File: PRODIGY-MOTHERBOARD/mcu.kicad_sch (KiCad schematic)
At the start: 19 parts, among them J1 USB_C_Receptacle, J2 Bus_M.2_Socket_B, SW1 SW_Push_Dual_x2

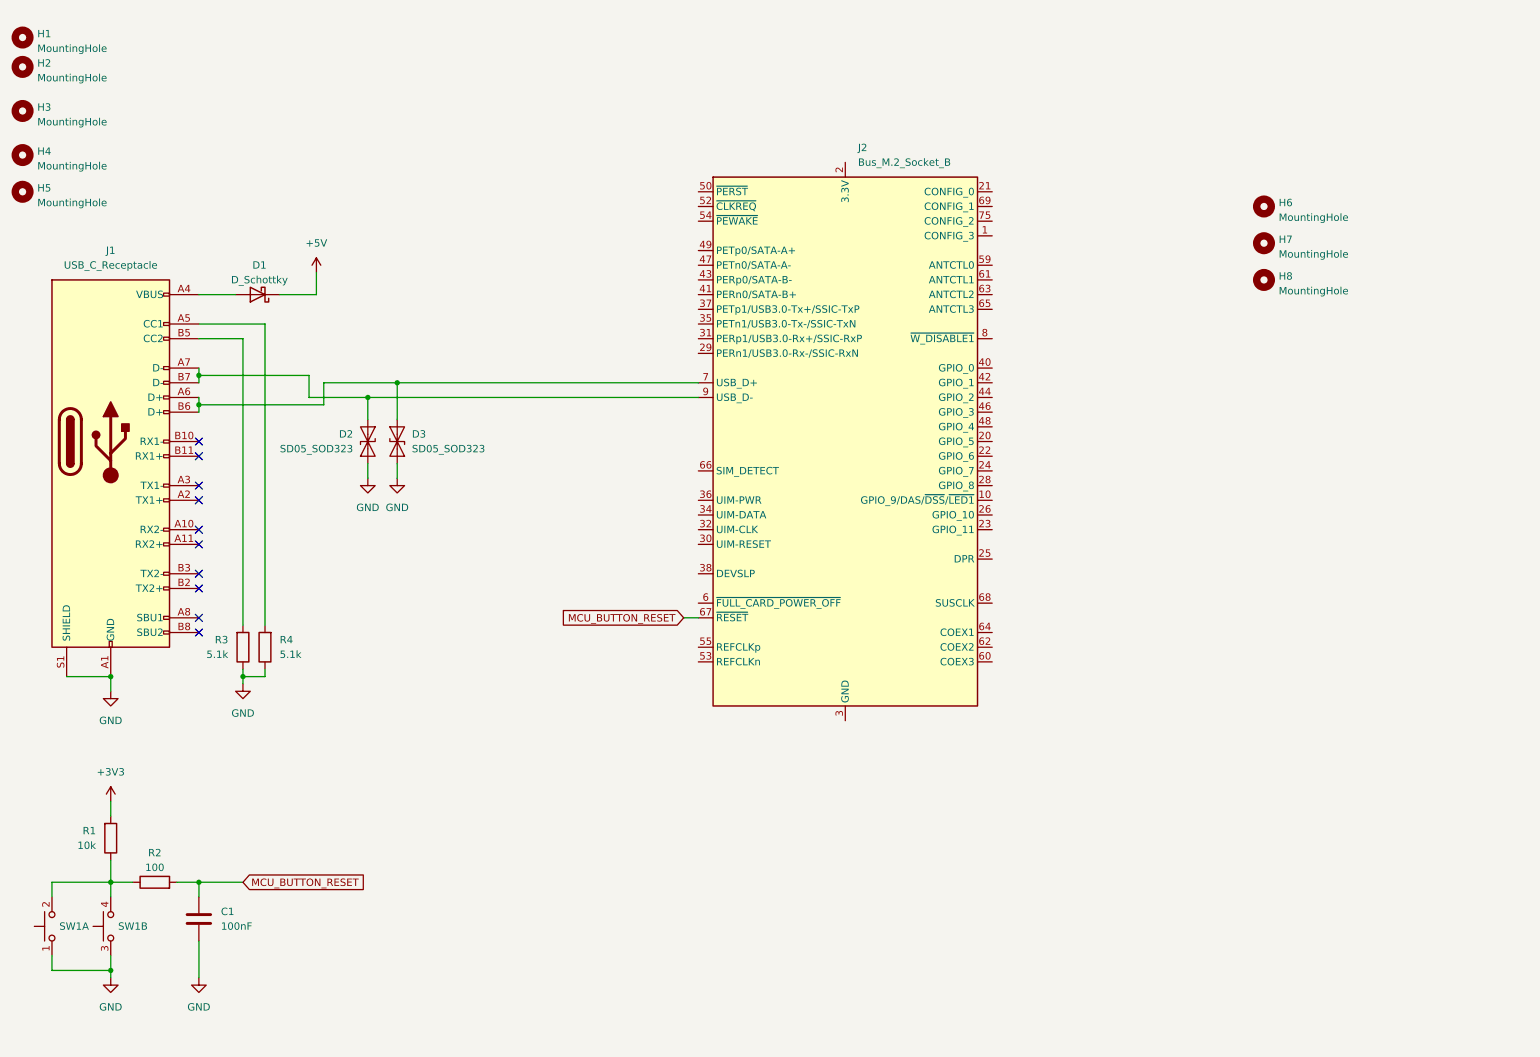
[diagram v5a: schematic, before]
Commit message: Added pins to MCU. Added Decoder for SPI SS-Multiplexing.
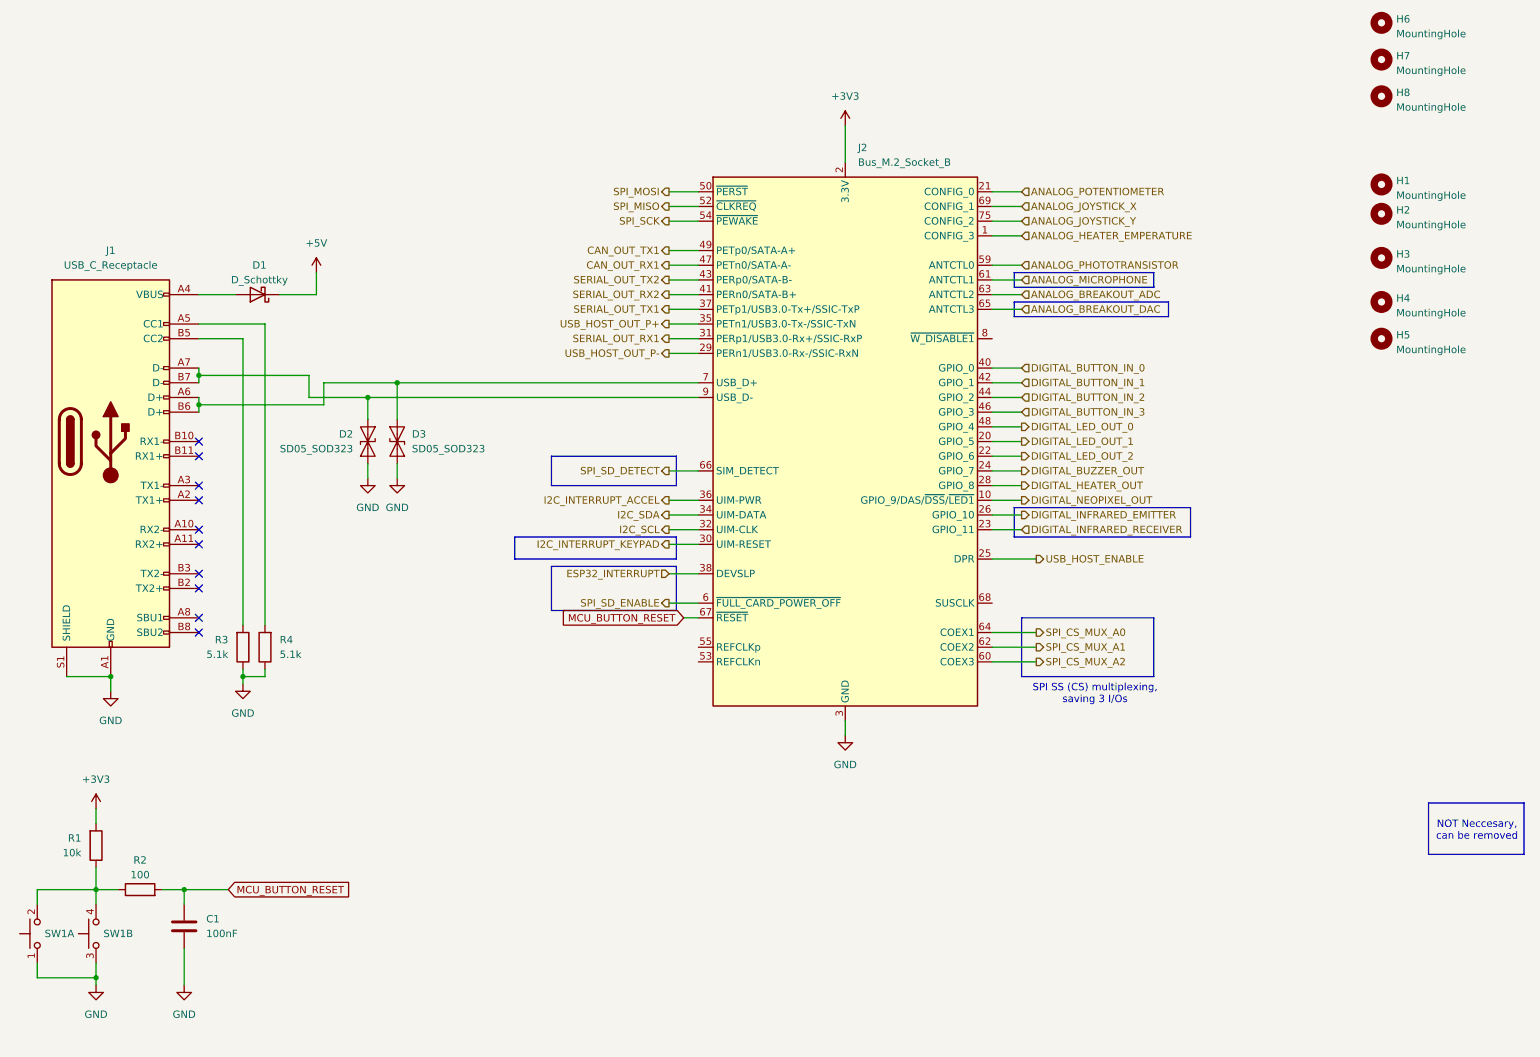
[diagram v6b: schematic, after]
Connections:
- net +3V3: now also J2.2 (3.3V), J2.4 (3.3V), J2.70 (3.3V), J2.72 (3.3V), J2.74 (3.3V)
- net GND: now also J2.11 (GND), J2.27 (GND), J2.3 (GND), J2.33 (GND), J2.39 (GND), J2.45 (GND), J2.5 (GND), J2.51 (GND), J2.57 (GND), J2.71 (GND), J2.73 (GND)
- net ANALOG_HEATER_EMPERATURE: now reaches J2.1 (CONFIG_3)
- net DIGITAL_NEOPIXEL_OUT: now reaches J2.10 (GPIO_9/DAS/~{DSS}/~{LED1})
- net DIGITAL_LED_OUT_1: now reaches J2.20 (GPIO_5)
- net ANALOG_POTENTIOMETER: now reaches J2.21 (CONFIG_0)
- net DIGITAL_LED_OUT_2: now reaches J2.22 (GPIO_6)
- net DIGITAL_INFRARED_RECEIVER: now reaches J2.23 (GPIO_11)
- net DIGITAL_BUZZER_OUT: now reaches J2.24 (GPIO_7)
- net USB_HOST_ENABLE: now reaches J2.25 (DPR)
- net DIGITAL_INFRARED_EMITTER: now reaches J2.26 (GPIO_10)
- net DIGITAL_HEATER_OUT: now reaches J2.28 (GPIO_8)
- net USB_HOST_OUT_P-: now reaches J2.29 (PERn1/USB3.0-Rx-/SSIC-RxN)
- net I2C_INTERRUPT_KEYPAD: now reaches J2.30 (UIM-RESET)
- net SERIAL_OUT_RX1: now reaches J2.31 (PERp1/USB3.0-Rx+/SSIC-RxP)
- net I2C_SCL: now reaches J2.32 (UIM-CLK)
- net I2C_SDA: now reaches J2.34 (UIM-DATA)
- net USB_HOST_OUT_P+: now reaches J2.35 (PETn1/USB3.0-Tx-/SSIC-TxN)
- net I2C_INTERRUPT_ACCEL: now reaches J2.36 (UIM-PWR)
- net SERIAL_OUT_TX1: now reaches J2.37 (PETp1/USB3.0-Tx+/SSIC-TxP)
- net ESP32_INTERRUPT: now reaches J2.38 (DEVSLP)
- net DIGITAL_BUTTON_IN_0: now reaches J2.40 (GPIO_0)
- net SERIAL_OUT_RX2: now reaches J2.41 (PERn0/SATA-B+)
- net DIGITAL_BUTTON_IN_1: now reaches J2.42 (GPIO_1)
- net SERIAL_OUT_TX2: now reaches J2.43 (PERp0/SATA-B-)
- net DIGITAL_BUTTON_IN_2: now reaches J2.44 (GPIO_2)
- net DIGITAL_BUTTON_IN_3: now reaches J2.46 (GPIO_3)
- net CAN_OUT_RX1: now reaches J2.47 (PETn0/SATA-A-)
- net DIGITAL_LED_OUT_0: now reaches J2.48 (GPIO_4)
- net CAN_OUT_TX1: now reaches J2.49 (PETp0/SATA-A+)
- net SPI_MOSI: now reaches J2.50 (~{PERST})
- net SPI_MISO: now reaches J2.52 (~{CLKREQ})
- net SPI_SCK: now reaches J2.54 (~{PEWAKE})
- net ANALOG_PHOTOTRANSISTOR: now reaches J2.59 (ANTCTL0)
- net SPI_SD_ENABLE: now reaches J2.6 (~{FULL_CARD_POWER_OFF})
- net SPI_CS_MUX_A2: now reaches J2.60 (COEX3)
- net ANALOG_MICROPHONE: now reaches J2.61 (ANTCTL1)
- net SPI_CS_MUX_A1: now reaches J2.62 (COEX2)
- net ANALOG_BREAKOUT_ADC: now reaches J2.63 (ANTCTL2)
- net SPI_CS_MUX_A0: now reaches J2.64 (COEX1)
- net ANALOG_BREAKOUT_DAC: now reaches J2.65 (ANTCTL3)
- net SPI_SD_DETECT: now reaches J2.66 (SIM_DETECT)
- net ANALOG_JOYSTICK_X: now reaches J2.69 (CONFIG_1)
- net ANALOG_JOYSTICK_Y: now reaches J2.75 (CONFIG_2)
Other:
- note added: "NOT Neccesary, can be removed"
- note added: "SPI SS (CS) multiplexing, saving 3 I/Os"
- moved on the sheet: C1, H1, H2, H3, H4, H5, H6, H7, H8, R1, R2, SW1A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

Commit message: Added proper debounce filter elements to buttons.
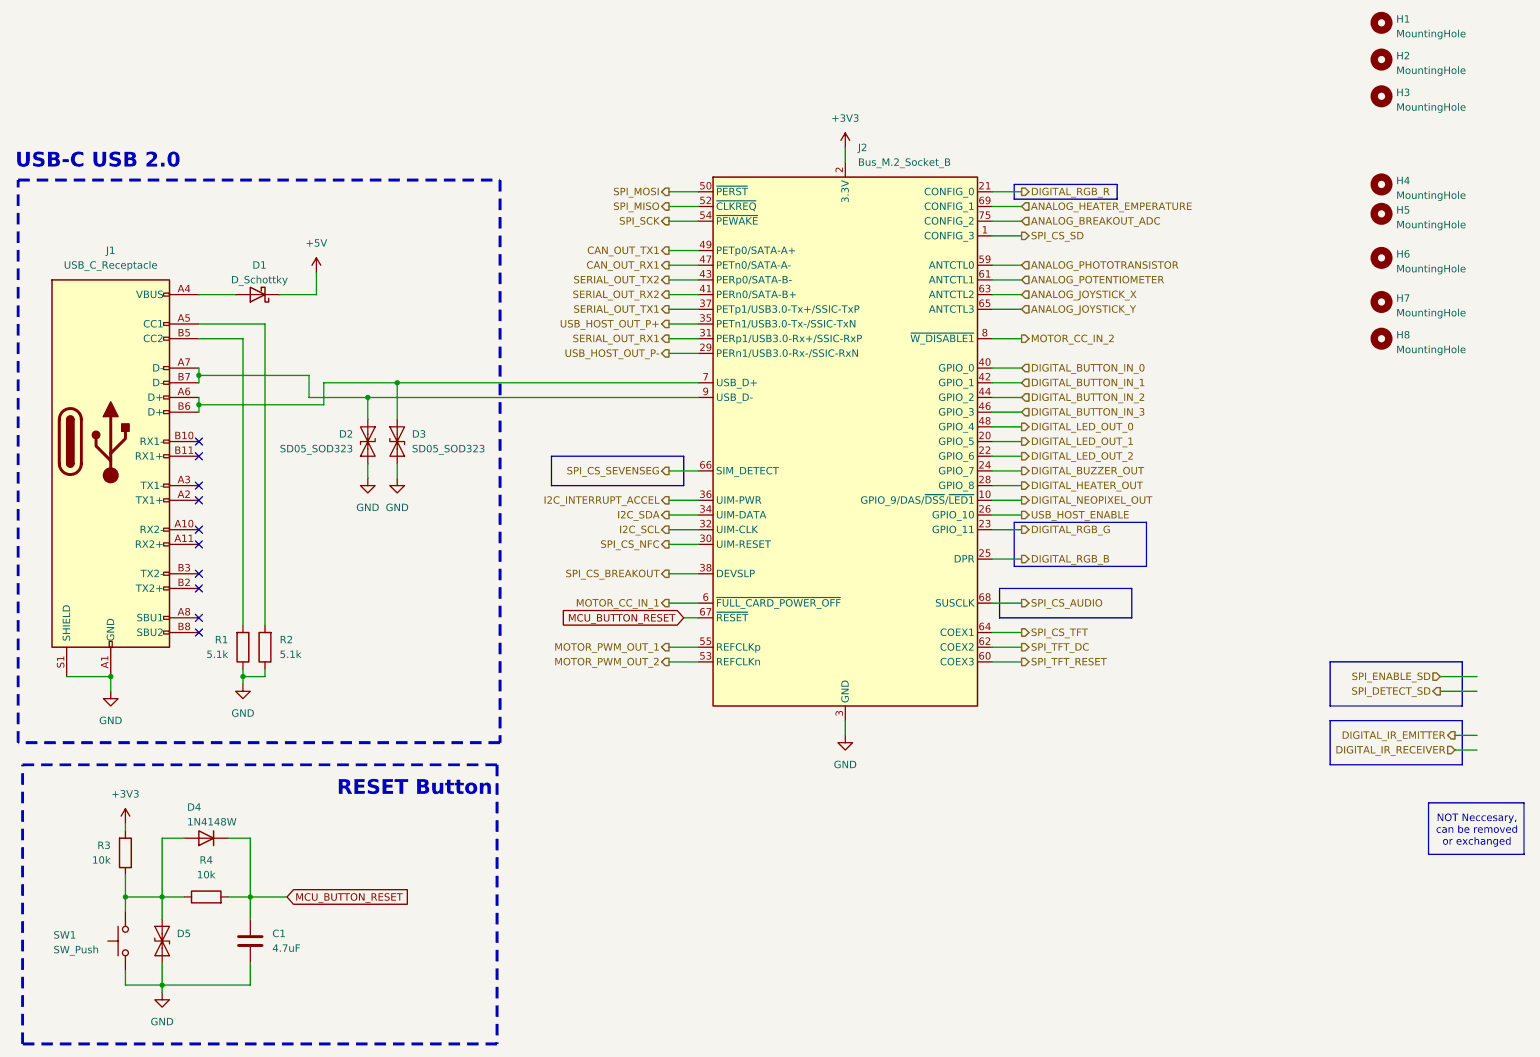
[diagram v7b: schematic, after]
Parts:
- removed R1: 10k, Resistor_SMD:R_0603_1608Metric, symbol Device:R
- removed R2: 100, Resistor_SMD:R_0603_1608Metric, symbol Device:R
- removed SW1: SW_Push_Dual_x2, symbol Switch:SW_Push_Dual_x2
- added D4: 1N4148W, Diode_SMD:D_SOD-123, symbol Diode:1N4148W
- added D5: SD05_SOD323, Diode_SMD:D_SOD-323, symbol Diode:SD05_SOD323
- added R3, R4: 10k, Resistor_SMD:R_0603_1608Metric, symbol Device:R
- added SW1: SW_Push, Button_Switch_SMD:SW_Push_1P1T_NO_CK_KMR2, symbol Switch:SW_Push
- C1: value 100nF -> 4.7uF
- renumbered H6 to H1, H7 to H2, H8 to H3, H1 to H4, H2 to H5, H3 to H6, H4 to H7, H5 to H8, R3 to R1, R4 to R2
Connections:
- net ANALOG_BREAKOUT_DAC is gone; now on net ANALOG_JOYSTICK_Y: J2.65 (ANTCTL3)
- net ANALOG_MICROPHONE is gone; now on net ANALOG_POTENTIOMETER: J2.61 (ANTCTL1)
- net DIGITAL_INFRARED_EMITTER is gone; now on net USB_HOST_ENABLE: J2.26 (GPIO_10)
- net +3V3: now also R3.2
- net ANALOG_BREAKOUT_ADC: now also J2.75 (CONFIG_2); no longer J2.63 (ANTCTL2)
- net ANALOG_HEATER_EMPERATURE: now also J2.69 (CONFIG_1); no longer J2.1 (CONFIG_3)
- net ANALOG_JOYSTICK_X: now also J2.63 (ANTCTL2); no longer J2.69 (CONFIG_1)
- net ANALOG_JOYSTICK_Y: no longer J2.75 (CONFIG_2)
- net ANALOG_POTENTIOMETER: no longer J2.21 (CONFIG_0)
- net GND: now also D5.1 (A1), SW1.1
- net MCU_BUTTON_RESET: now also D4.1 (K), R4.2
- net USB_HOST_ENABLE: no longer J2.25 (DPR)
- net MOTOR_PWM_OUT_2: now reaches J2.53 (REFCLKn)
- net MOTOR_PWM_OUT_1: now reaches J2.55 (REFCLKp)
- net SPI_CS_AUDIO: now reaches J2.68 (SUSCLK)
- net MOTOR_CC_IN_2: now reaches J2.8 (~{W_DISABLE1})
- net DIGITAL_INFRARED_RECEIVER renamed DIGITAL_RGB_G
- net ESP32_INTERRUPT renamed SPI_CS_BREAKOUT
- net I2C_INTERRUPT_KEYPAD renamed SPI_CS_NFC
- net SPI_CS_MUX_A0 renamed SPI_CS_TFT
- net SPI_CS_MUX_A1 renamed SPI_TFT_DC
- net SPI_CS_MUX_A2 renamed SPI_TFT_RESET
- net SPI_SD_DETECT renamed SPI_CS_SEVENSEG
- net SPI_SD_ENABLE renamed MOTOR_CC_IN_1
- new net: D4.2 (A), D5.2 (A2), R3.1, R4.1, SW1.2
- new net DIGITAL_RGB_B: J2.25 (DPR)
- new net DIGITAL_RGB_R: J2.21 (CONFIG_0)
- new net SPI_CS_SD: J2.1 (CONFIG_3)
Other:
- note added: "NOT Neccesary, can be removed or exchanged"
- note added: "RESET Button"
- note added: "USB-C USB 2.0"
- note removed: "NOT Neccesary, can be removed"
- note removed: "SPI SS (CS) multiplexing, saving 3 I/Os"

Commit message: Submitted V0 for evaluation. Avaiting feedback.
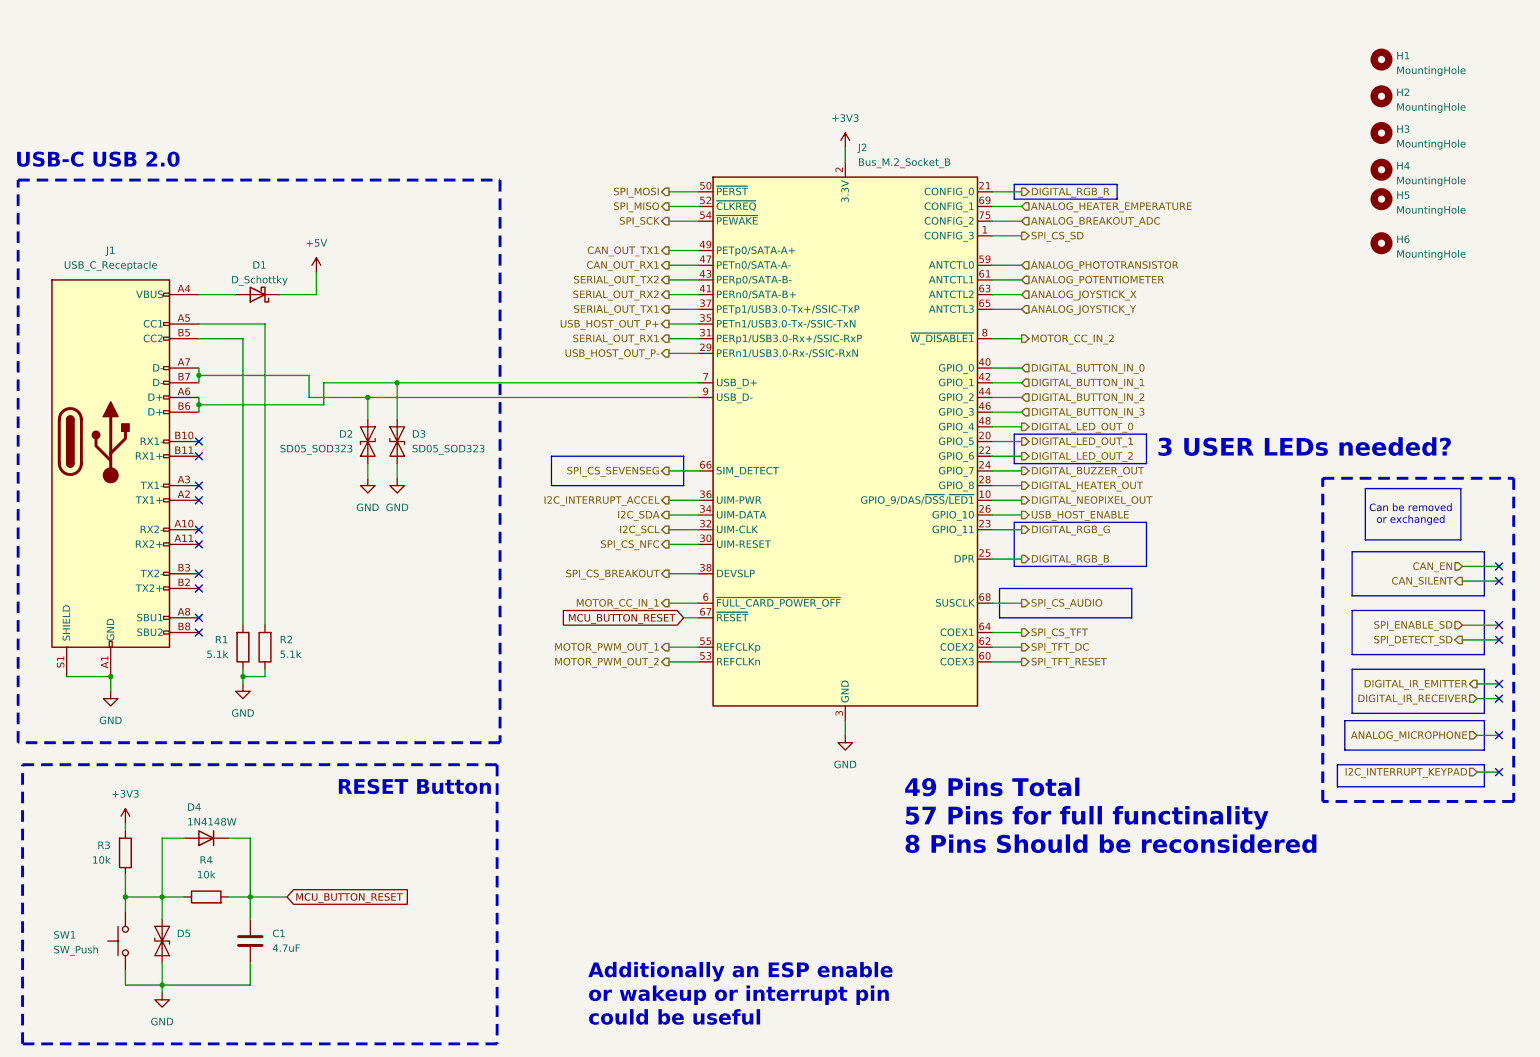
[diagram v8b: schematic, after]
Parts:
- removed H7, H8: MountingHole, MountingHole:MountingHole_3.2mm_M3_ISO7380_Pad_TopBottom, symbol Mechanical:MountingHole
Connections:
- no-connect marks 10 -> 18
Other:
- note added: "3 USER LEDs needed?"
- note added: "49 Pins Total 57 Pins for full functinality 8 Pins Should be reconsidered"
- note added: "Additionally an ESP enable or wakeup or interrupt pin could be useful"
- note added: "Can be removed or exchanged"
- note removed: "NOT Neccesary, can be removed or exchanged"
- moved on the sheet: H1, H2, H3, H4, H5, H6
